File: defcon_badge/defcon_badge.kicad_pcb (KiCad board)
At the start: 4 copper layers, 86 x 54 mm, 80 parts, among them J10 USB_C_Receptacle_GCT_USB4085, J11 JST-PH 2P, J20 PJ-320A, J30 SAO 2x3, J31 microSD, J32 UART debug, J33 Dev/SWD header, SW1 SS-12D00, SW20 TS-1187A, SW21 TS-1187A, SW22 TS-1187A, U10 TP4056, U11 ME6211C33M5G, U2 W25Q16JVUXIQ, U20 TM8211, U21 TDA1308, U3 RP2040, U30 TSOP4838, Y1 ABM8-272-T3

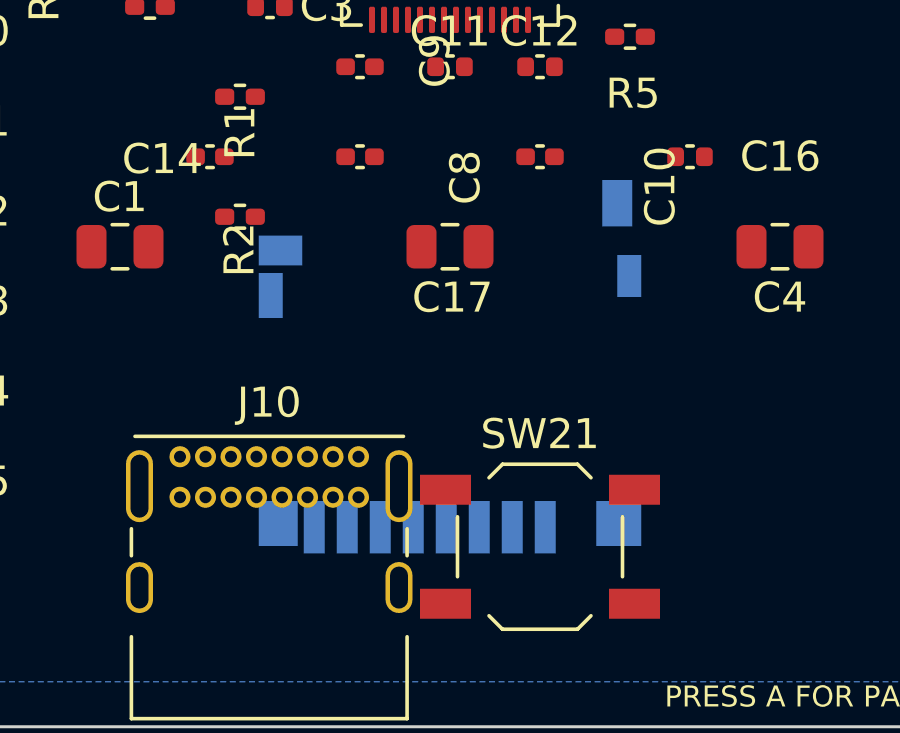
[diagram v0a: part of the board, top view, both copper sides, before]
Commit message: iter(25): rotate microSD 180° on back — card insertion from bottom edge
The 0° orientation had the card slot opening upward (into the body of
the board), which is non-functional. Rotating 180° points the slot
opening toward the bottom edge of the board so the card can be
inserted from below.

Re-rendered docs/render_3d_bottom.png to show the updated orientation.

Co-Authored-By: Claude Opus 4.7 (1M context) <noreply@anthropic.com>
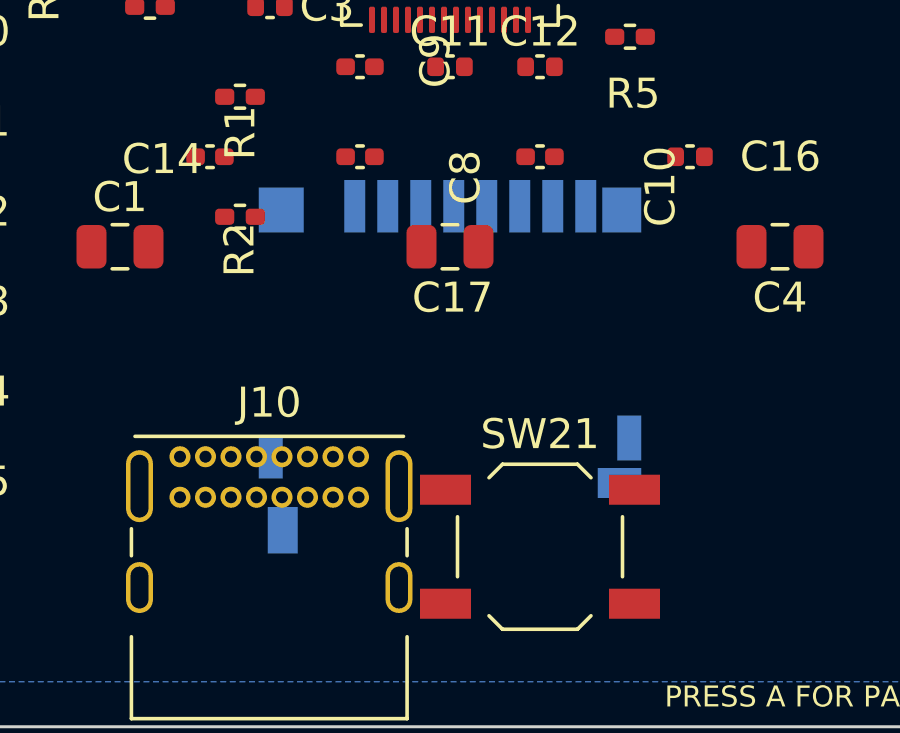
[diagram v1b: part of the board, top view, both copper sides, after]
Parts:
- turned J31 to 180 degrees

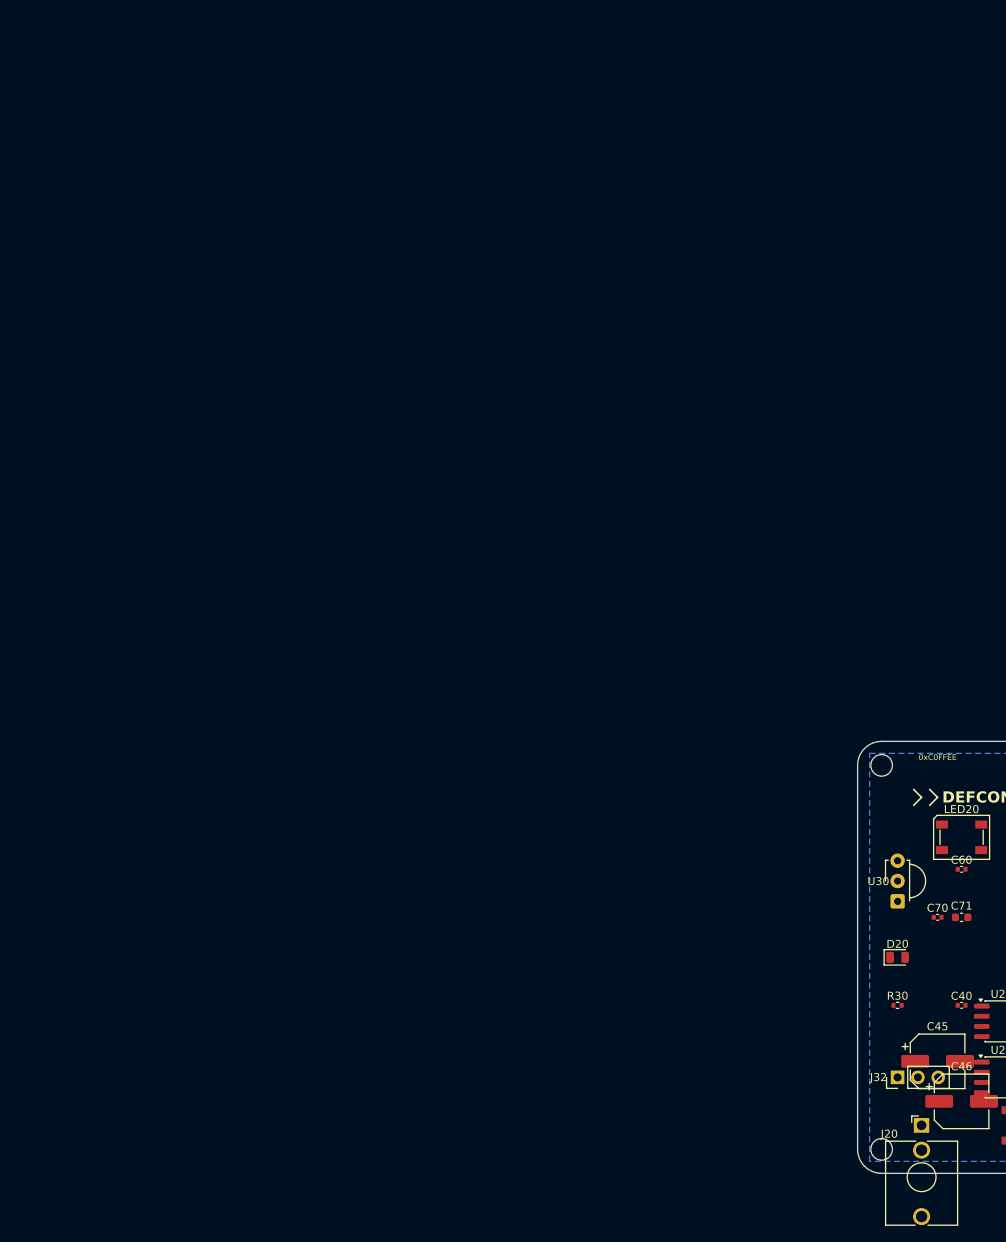
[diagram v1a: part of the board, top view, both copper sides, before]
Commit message: fix(J20): swap audio jack to Amphenol 10038075-D0P SMD horizontal
The original WQP-PJ398SM (Thonkiconn) footprint was a Value/footprint
mismatch (schematic said PJ-320A) AND had no 3D model — the jack body
didn't render. Replaced with the user-provided Amphenol 10038075-D0P
SMD stereo jack:

- Imported AMPHENOL_10038075-D0P.kicad_mod into defcon_badge.pretty/
  (auto-upgraded to KiCad 10 format via 'kicad-cli fp upgrade')
- Imported 10038075-D0P.step into defcon_badge.3dshapes/
- Added (model ...) reference to the .kicad_mod pointing at the .step
  via ${KIPRJMOD}/defcon_badge.3dshapes/
- Removed old J20 from PCB, inserted new footprint at (108, 128)
- Net assignments: pad 1 -> /Audio/JACK_R, pad 2 -> GND, pad 3 ->
  /Audio/JACK_L (educated guess from pad geometry; swap if datasheet
  disagrees)
- 3D render now shows a real silver metal jack body extending off the
  bottom-left edge of the board

Co-Authored-By: Claude Opus 4.7 (1M context) <noreply@anthropic.com>
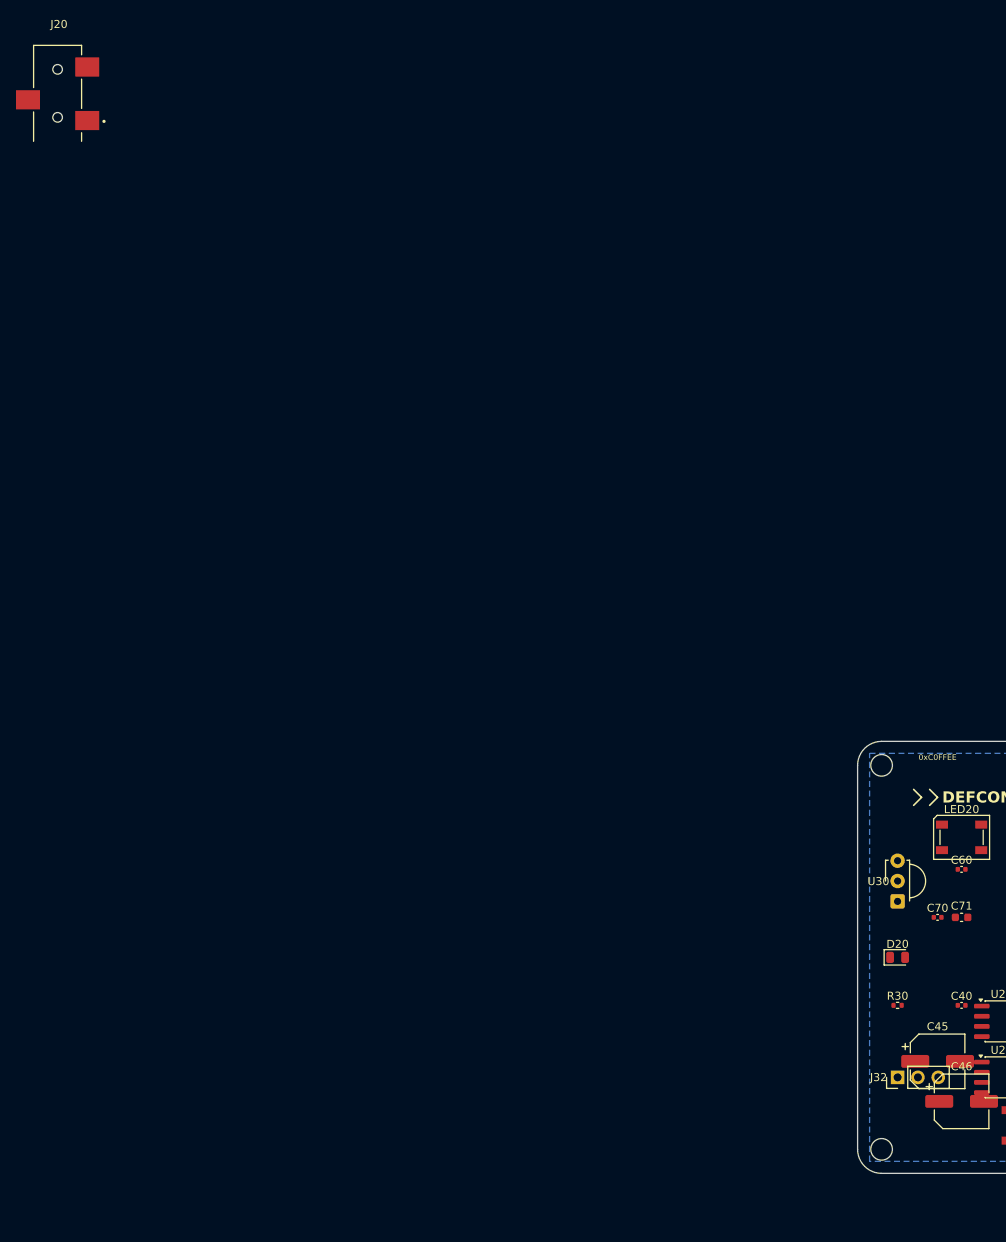
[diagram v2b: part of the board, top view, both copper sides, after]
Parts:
- J20: value PJ-320A -> AMPHENOL_10038075-D0P; footprint Connector_Audio:Jack_3.5mm_QingPu_WQP-PJ398SM_Vertical_CircularHoles -> RP2040_minimal:AMPHENOL_10038075-D0P
- moved J20 167.5 mm to (0.00, 0.00)

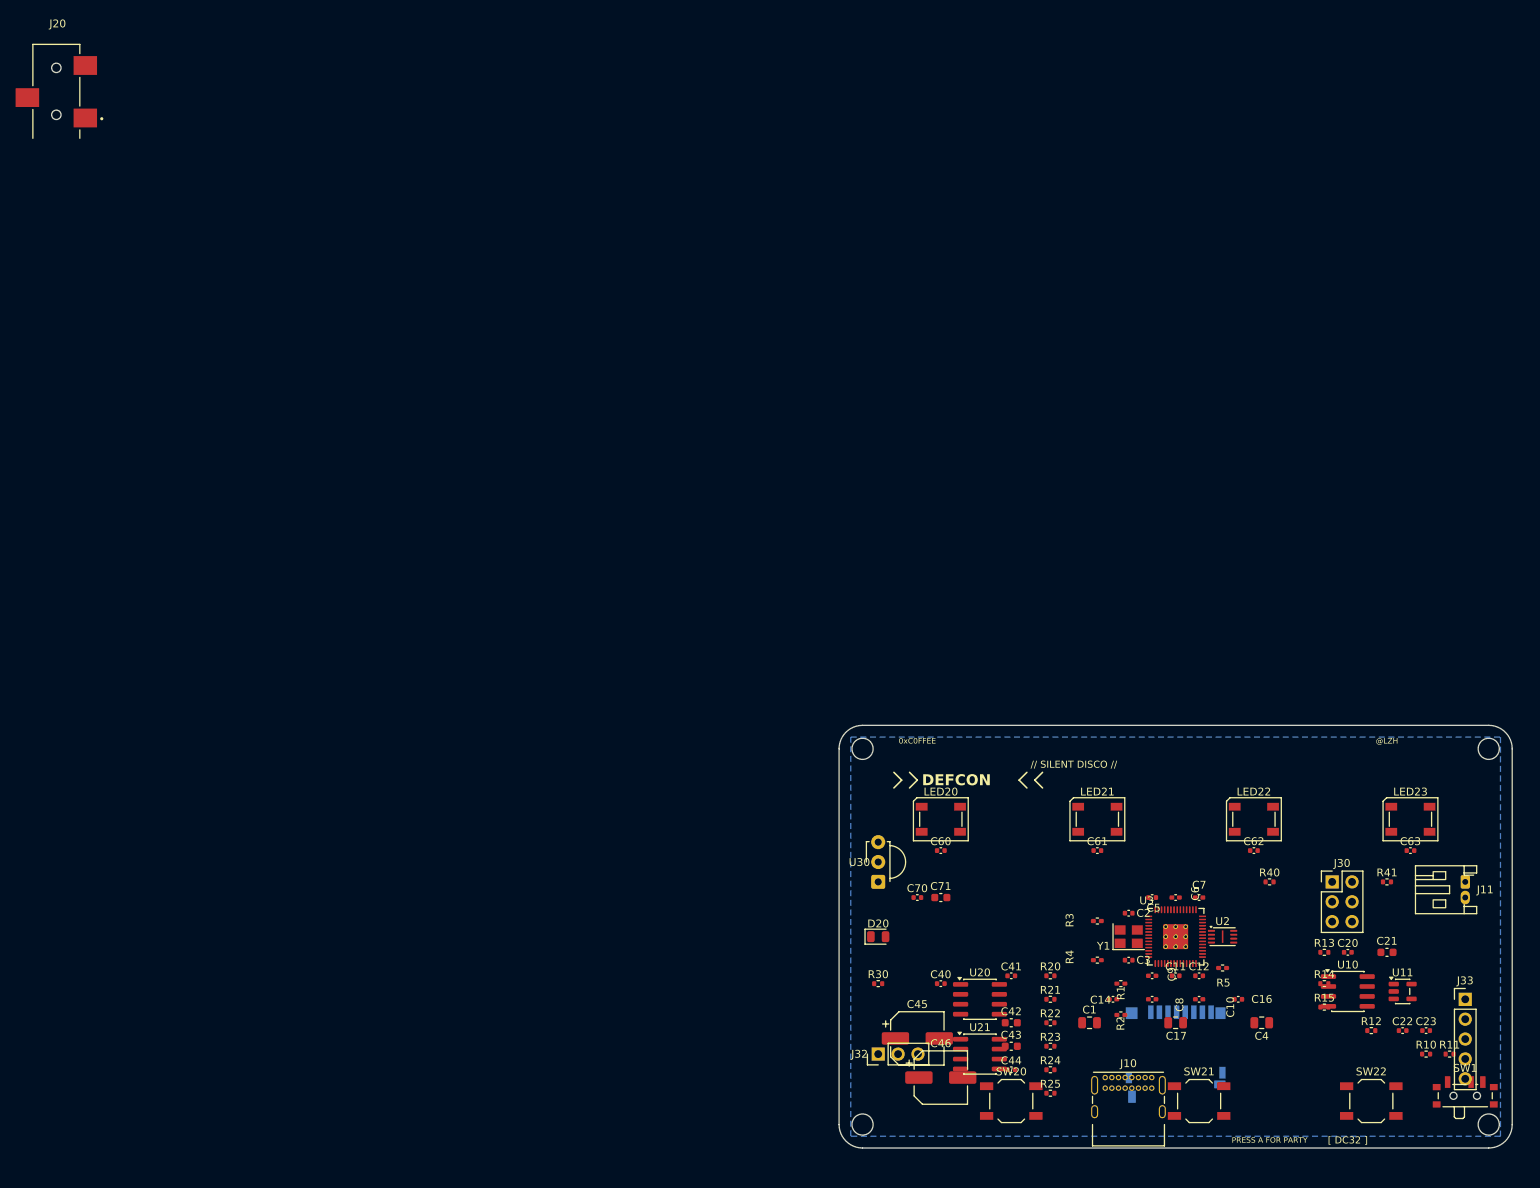
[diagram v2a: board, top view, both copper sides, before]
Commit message: iter(30): sawtooth edges for board pairing
New tools/set_outline_v2.py rewrites Edge.Cuts with sawtooth profile on
the left and right edges. Period 5mm, depth 1.5mm. Phase offset of T/2
between left and right means when two boards meet edge-to-edge, A's
right-edge peaks slot exactly into B's left-edge valleys.

The IR pair will sit at one chosen peak/valley pair (default y=108.75):
D20 IR LED at a right-edge peak (clear sightline), U30 receiver at a
left-edge valley (slightly recessed). When boards mate, the two parts
face each other across a ~1mm air gap inside the void created by the
mated peaks — ready for a 3D-printed light cover.

Top + bottom edges remain straight: top is the LED row, bottom is the
USB/audio/button row, no pairing happens vertically.

Iter 31 next: depopulate the board and stage components off-board so
we can rebuild a clean floor plan with all 7 of the user's screenshot
issues fixed.

Co-Authored-By: Claude Opus 4.7 (1M context) <noreply@anthropic.com>
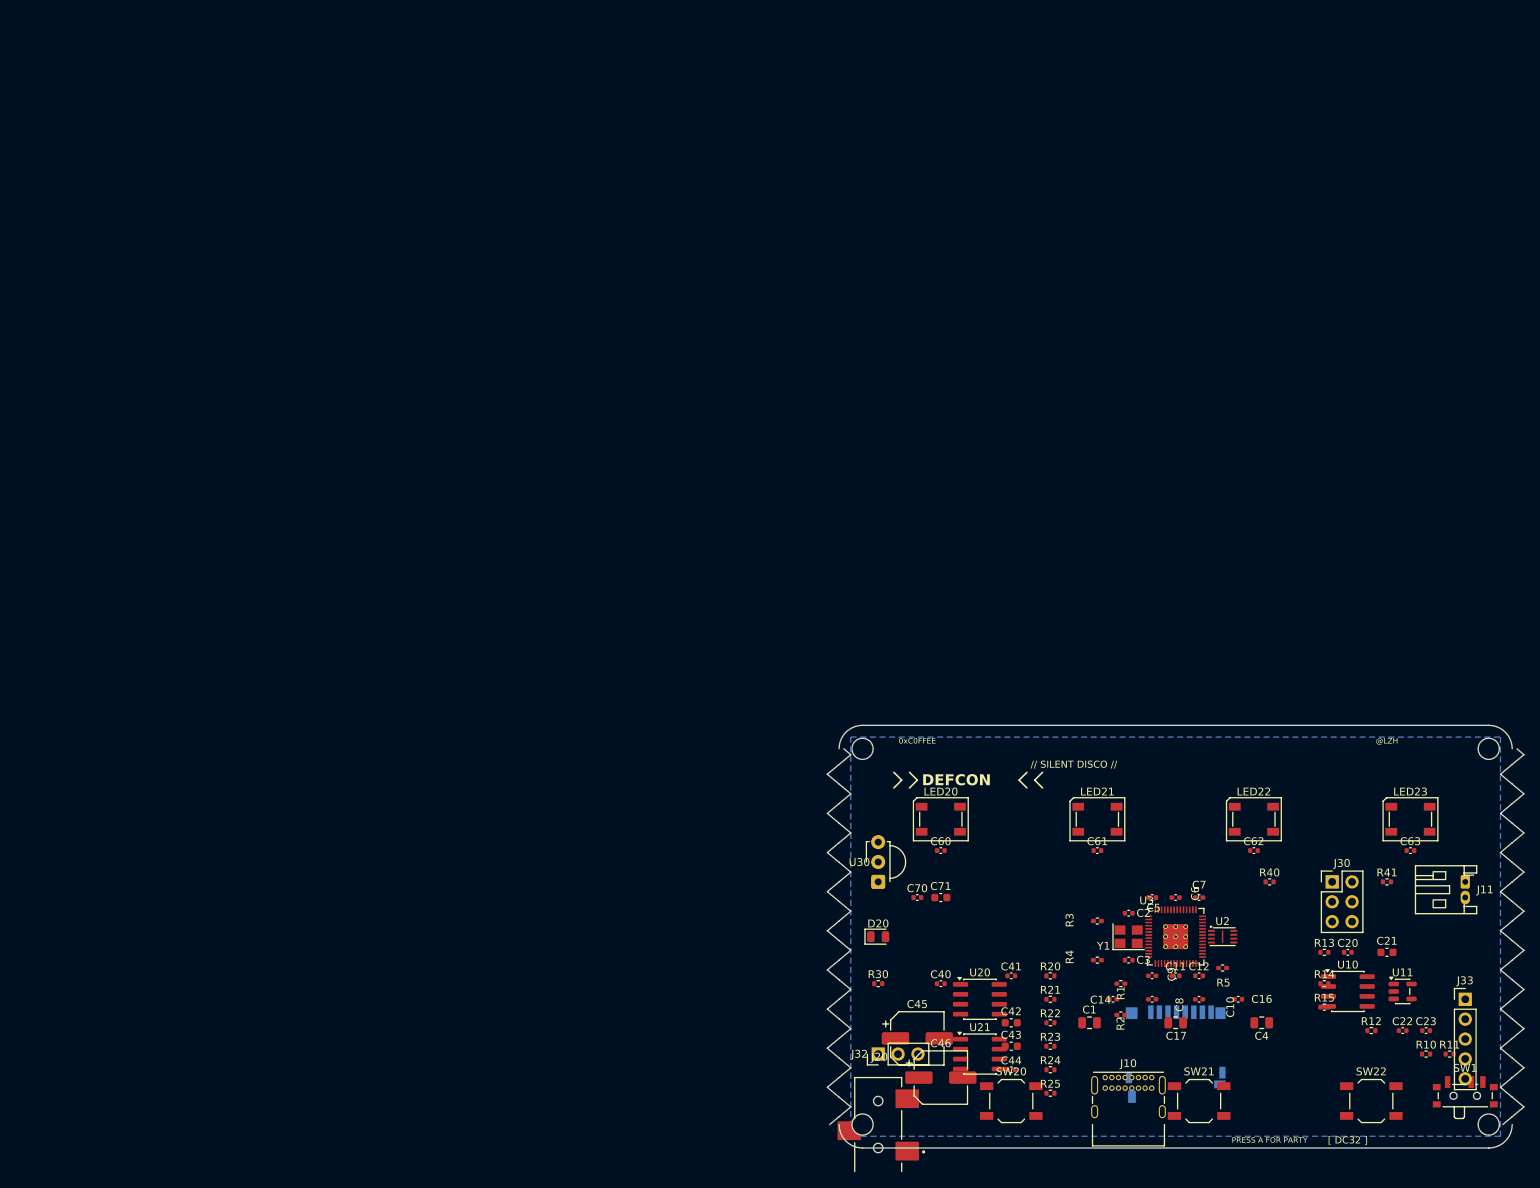
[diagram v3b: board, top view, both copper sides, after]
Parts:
- moved J20 168.7 mm to (105.0, 132.0)
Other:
- board size 86 x 54 mm -> 89 x 54 mm
